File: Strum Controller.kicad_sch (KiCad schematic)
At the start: 18 parts, among them J1 USB_C_Receptacle_USB2.0, U1 RP2040, U2 NCP1117-3.3_SOT223

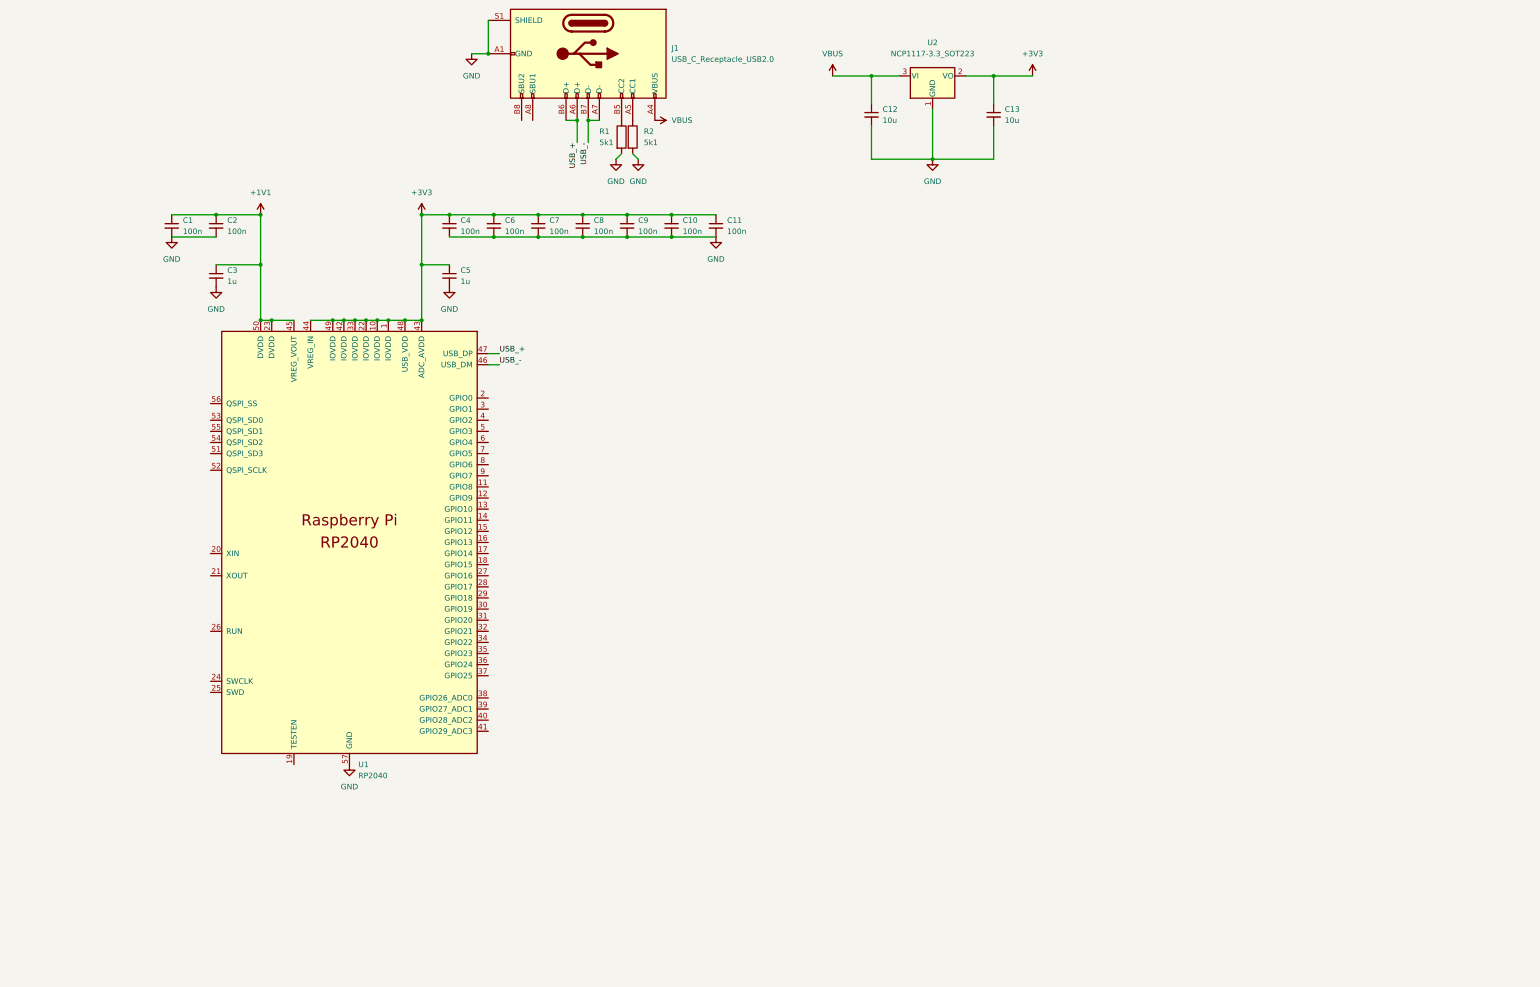
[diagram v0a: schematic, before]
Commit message: Restart design using modified RP2040 minimal design from RasPi Foundation
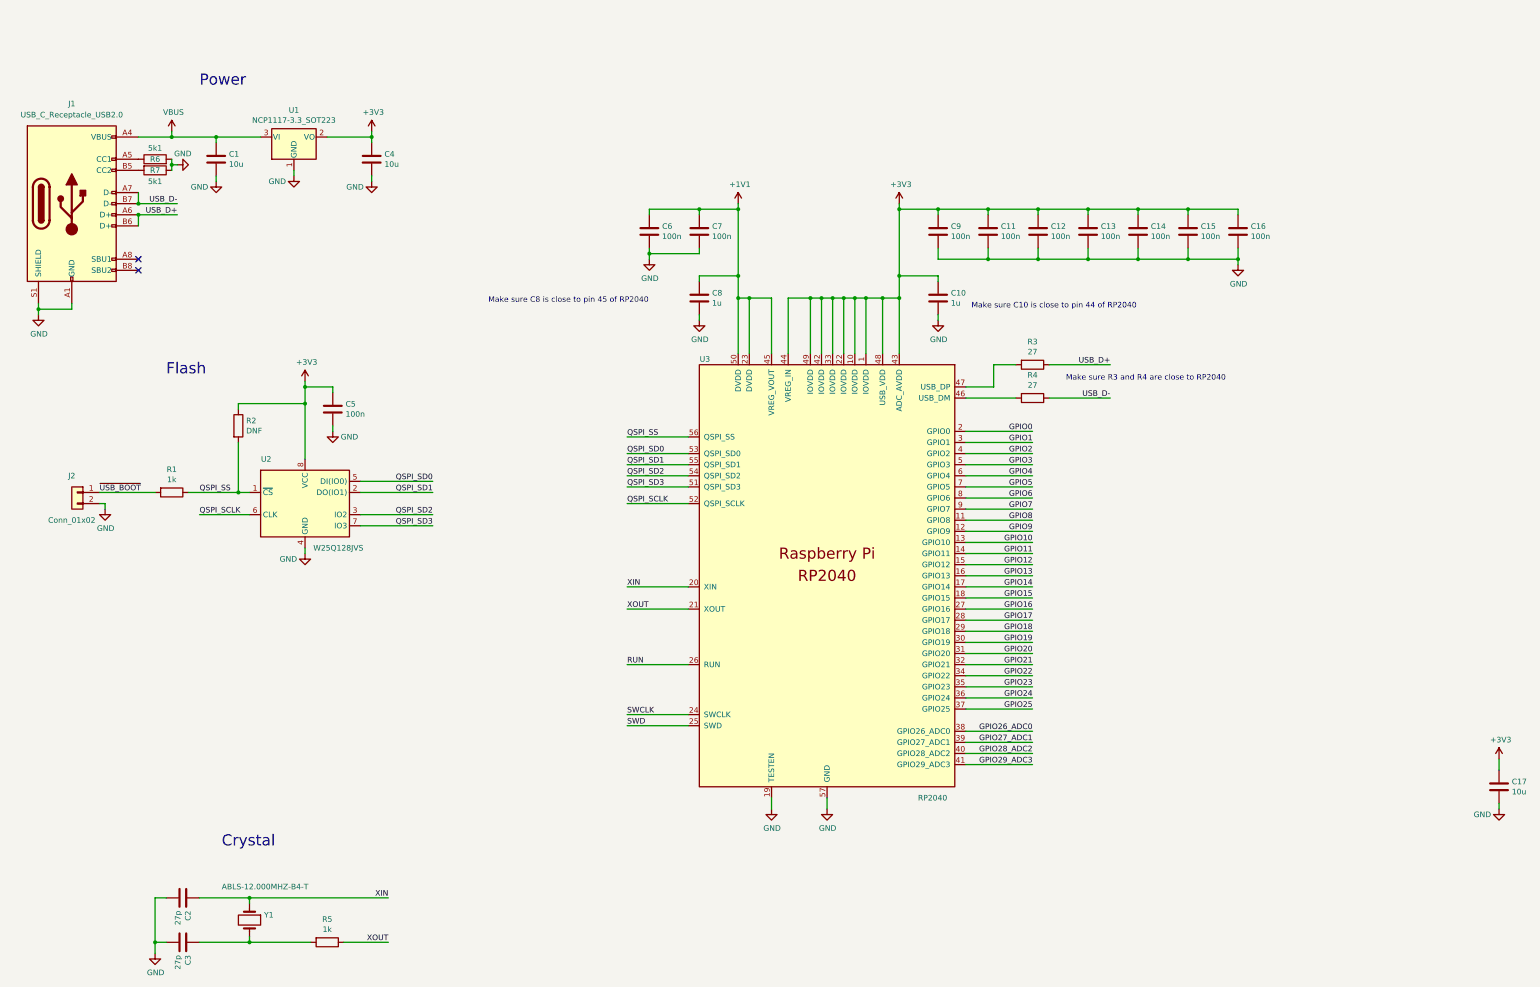
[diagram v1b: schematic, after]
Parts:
- removed C1, C10, C11, C2, C4, C6, C7, C8, C9: 100n, Capacitor_SMD:C_0402_1005Metric, symbol Device:C_Small
- removed C12, C13: 10u, Capacitor_SMD:C_0402_1005Metric, symbol Device:C_Small
- removed C3, C5: 1u, Capacitor_SMD:C_0402_1005Metric, symbol Device:C_Small
- removed U1: RP2040, kicad-rp2040:RP2040_QFN-56_EP_7x7_Pitch0.4mm_ThermalVias, symbol kicad-rp2040:RP2040
- removed U2: NCP1117-3.3_SOT223, Package_TO_SOT_SMD:SOT-223-3_TabPin2, symbol Regulator_Linear:NCP1117-3.3_SOT223
- added C1, C17, C4: 10u, Capacitor_SMD:C_0805_2012Metric, symbol Device:C
- added C10, C8: 1u, Capacitor_SMD:C_0402_1005Metric, symbol Device:C
- added C11, C12, C13, C14, C15, C16, C5, C6, C7, C9: 100n, Capacitor_SMD:C_0402_1005Metric, symbol Device:C
- added C2, C3: 27p, Capacitor_SMD:C_0402_1005Metric, symbol Device:C
- added J2: Conn_01x02, Connector_PinHeader_2.54mm:PinHeader_1x02_P2.54mm_Vertical, symbol Connector_Generic:Conn_01x02
- added R3, R4: 27, Resistor_SMD:R_0402_1005Metric, symbol Device:R
- added R5: 1k, Resistor_SMD:R_0402_1005Metric, symbol Device:R
- added R6, R7: 5k1, Resistor_SMD:R_0402_1005Metric, symbol Device:R
- added U1: NCP1117-3.3_SOT223, Package_TO_SOT_SMD:SOT-223-3_TabPin2, symbol Regulator_Linear:NCP1117-3.3_SOT223
- added U2: W25Q128JVS, Package_SO:SOIC-8_5.275x5.275mm_P1.27mm, symbol Memory_Flash:W25Q128JVS
- added U3: RP2040, kicad-rp2040:RP2040_QFN-56_EP_7x7_Pitch0.4mm_ThermalVias, symbol kicad-rp2040:RP2040
- added Y1: ABLS-12.000MHZ-B4-T, Crystal:Crystal_SMD_HC49-SD, symbol Device:Crystal
- J1: footprint Connector_USB:USB_C_Receptacle_HRO_TYPE-C-31-M-12 -> Connector_USB:USB_C_Receptacle_JAE_DX07S016JA1R1500
- R1: value 5k1 -> 1k; footprint Resistor_SMD:R_0201_0603Metric -> Resistor_SMD:R_0402_1005Metric
- R2: value 5k1 -> DNF; footprint Resistor_SMD:R_0201_0603Metric -> Resistor_SMD:R_0402_1005Metric
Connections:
- net +1V1: now also C6.1, C7.1, C8.1, U3.23 (DVDD), U3.45 (VREG_VOUT), U3.50 (DVDD)
- net +3V3: now also R2.1, C10.1, C11.1, C12.1, C13.1, C14.1, C15.1, C16.1, C17.1, C4.1, C5.1, C9.1, U1.2 (VO), U2.8 (VCC), U3.1 (IOVDD), U3.10 (IOVDD), U3.22 (IOVDD), U3.33 (IOVDD), U3.42 (IOVDD), U3.43 (ADC_AVDD), U3.44 (VREG_IN), U3.48 (USB_VDD), U3.49 (IOVDD)
- net GND: now also C1.2, C10.2, C11.2, C12.2, C13.2, C14.2, C15.2, C16.2, C17.2, C2.2, C3.2, C4.2, C5.2, C6.2, C7.2, C8.2, C9.2, J2.2 (Pin_2), R6.2, R7.1, U1.1 (GND), U2.4 (GND), U3.19 (TESTEN), U3.57 (GND); no longer R1.2, R2.2
- net VBUS: now also C1.1, U1.3 (VI)
- net at J1.A5 (CC1): now also R6.1; no longer R2.1
- net at J1.B5 (CC2): now also R7.2; no longer R1.1
- net USB_+ renamed USB_D+
- net USB_D+: now also R3.1
- net USB_- renamed USB_D-
- net USB_D-: now also R4.1
- new net: R4.2, U3.46 (USB_DM)
- new net: R3.2, U3.47 (USB_DP)
- new net: C3.1, R5.2, Y1.2
- new net GPIO0: U3.2 (GPIO0)
- new net GPIO1: U3.3 (GPIO1)
- new net GPIO10: U3.13 (GPIO10)
- new net GPIO11: U3.14 (GPIO11)
- new net GPIO12: U3.15 (GPIO12)
- new net GPIO13: U3.16 (GPIO13)
- new net GPIO14: U3.17 (GPIO14)
- new net GPIO15: U3.18 (GPIO15)
- new net GPIO16: U3.27 (GPIO16)
- new net GPIO17: U3.28 (GPIO17)
- new net GPIO18: U3.29 (GPIO18)
- new net GPIO19: U3.30 (GPIO19)
- new net GPIO2: U3.4 (GPIO2)
- new net GPIO20: U3.31 (GPIO20)
- new net GPIO21: U3.32 (GPIO21)
- new net GPIO22: U3.34 (GPIO22)
- new net GPIO23: U3.35 (GPIO23)
- new net GPIO24: U3.36 (GPIO24)
- new net GPIO25: U3.37 (GPIO25)
- new net GPIO26_ADC0: U3.38 (GPIO26_ADC0)
- new net GPIO27_ADC1: U3.39 (GPIO27_ADC1)
- new net GPIO28_ADC2: U3.40 (GPIO28_ADC2)
- new net GPIO29_ADC3: U3.41 (GPIO29_ADC3)
- new net GPIO3: U3.5 (GPIO3)
- new net GPIO4: U3.6 (GPIO4)
- new net GPIO5: U3.7 (GPIO5)
- new net GPIO6: U3.8 (GPIO6)
- new net GPIO7: U3.9 (GPIO7)
- new net GPIO8: U3.11 (GPIO8)
- new net GPIO9: U3.12 (GPIO9)
- new net QSPI_SCLK: U2.6 (CLK), U3.52 (QSPI_SCLK)
- new net QSPI_SD0: U2.5 (DI(IO0)), U3.53 (QSPI_SD0)
- new net QSPI_SD1: U2.2 (DO(IO1)), U3.55 (QSPI_SD1)
- new net QSPI_SD2: U2.3 (IO2), U3.54 (QSPI_SD2)
- new net QSPI_SD3: U2.7 (IO3), U3.51 (QSPI_SD3)
- new net QSPI_SS: R1.1, R2.2, U2.1 (~{CS}), U3.56 (QSPI_SS)
- new net RUN: U3.26 (RUN)
- new net SWCLK: U3.24 (SWCLK)
- new net SWD: U3.25 (SWD)
- new net XIN: C2.1, U3.20 (XIN), Y1.1
- new net XOUT: R5.1, U3.21 (XOUT)
- new net ~{USB_BOOT}: J2.1 (Pin_1), R1.2
- no-connect marks 0 -> 2
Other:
- note added: "Crystal"
- note added: "Flash"
- note added: "Make sure C10 is close to pin 44 of RP2040"
- note added: "Make sure C8 is close to pin 45 of RP2040"
- note added: "Make sure R3 and R4 are close to RP2040"
- note added: "Power"
- company: (none) -> Raspberry Pi (Trading) Ltd
- title: (none) -> RP2040 Minimal Design Example

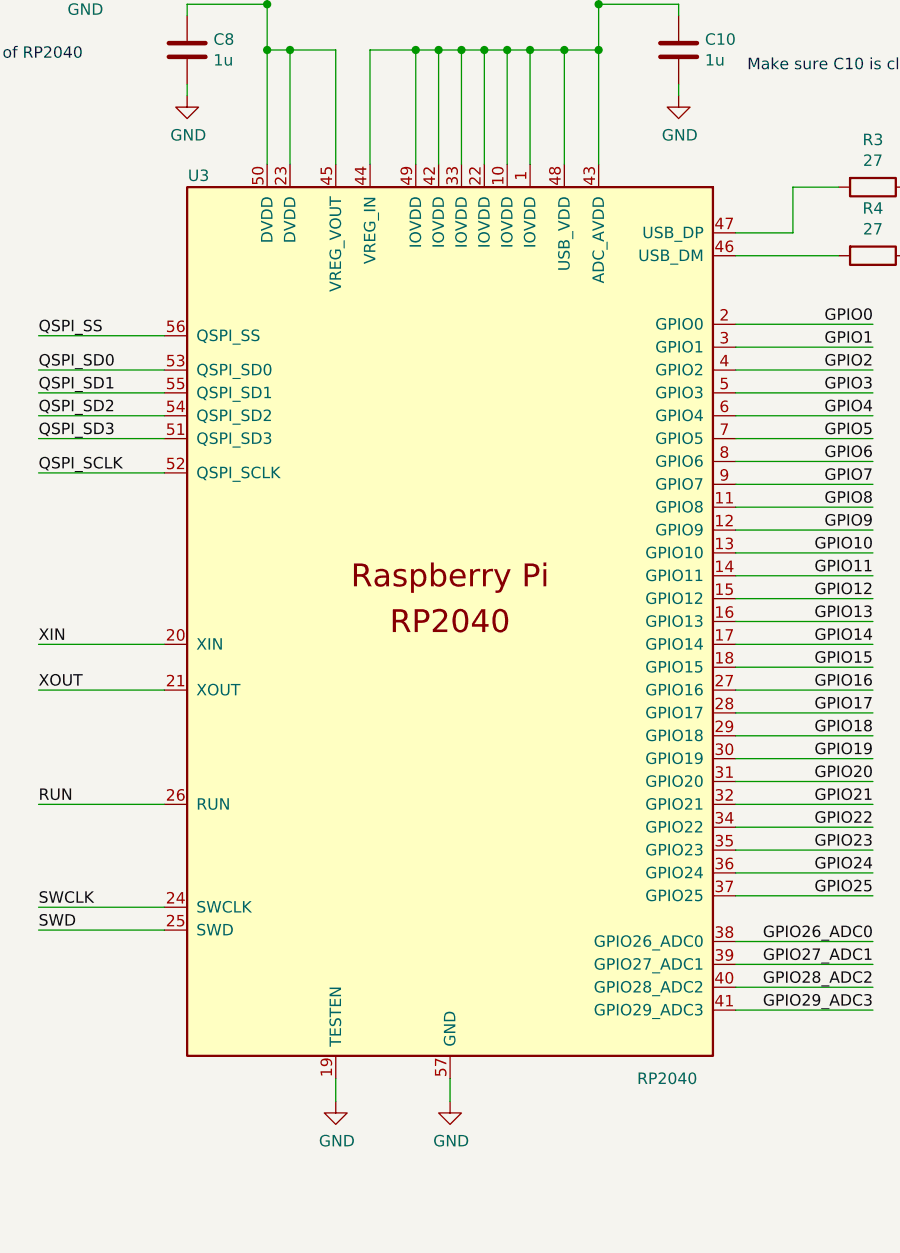
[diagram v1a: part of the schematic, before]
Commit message: Move to proper RP2040 library
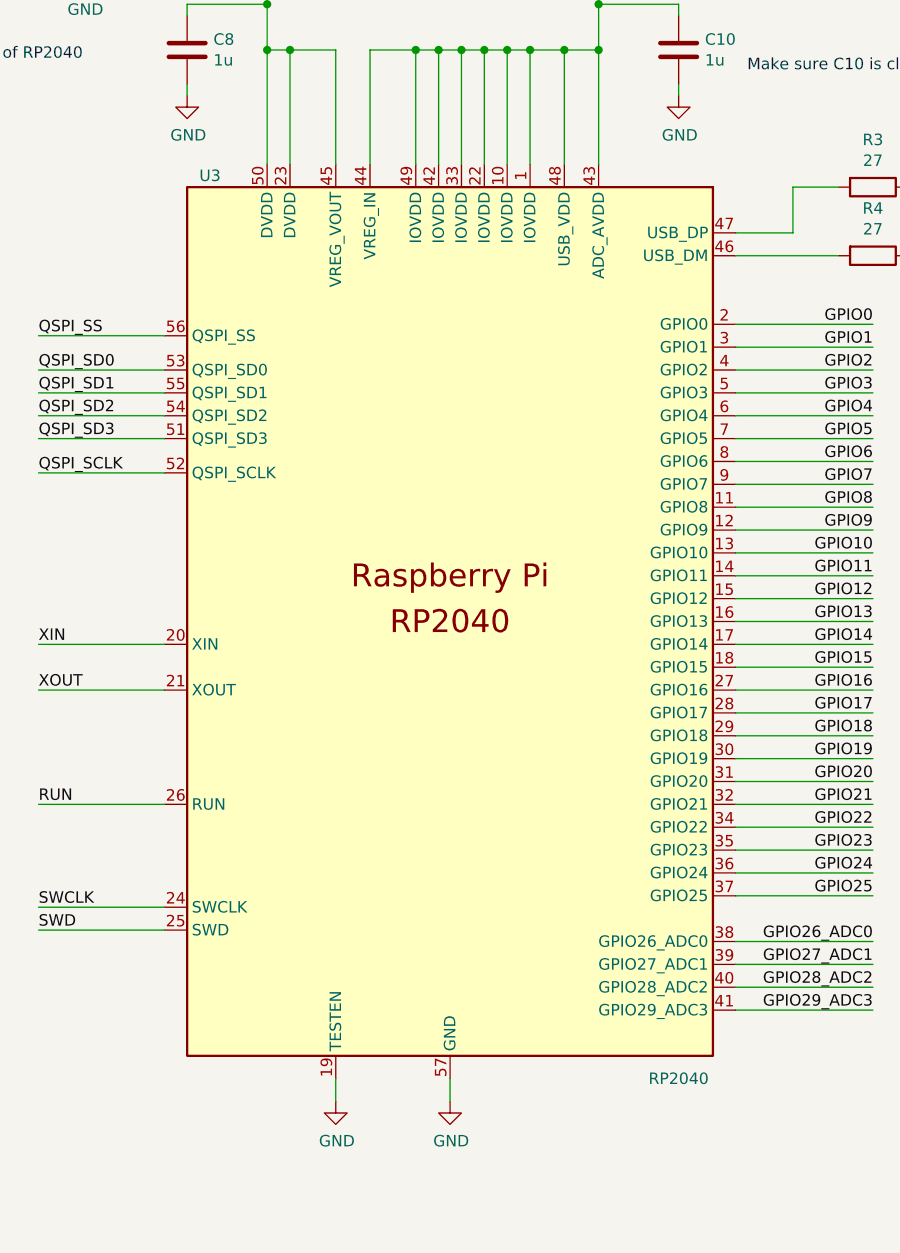
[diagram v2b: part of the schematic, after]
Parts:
- U3: footprint kicad-rp2040:RP2040_QFN-56_EP_7x7_Pitch0.4mm_ThermalVias -> kicad-lib-rp2040:QFN-56_EP_7x7_Pitch0.4mm_ThermalVias; symbol kicad-rp2040:RP2040 -> kicad-lib-rp2040:RP2040
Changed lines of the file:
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@@
     (effects (font (size 1.27 1.27)) (justify right bottom))
   )
-  (symbol (lib_id "kicad-rp2040:RP2040") (at 198.12 144.78 0) (unit 1)
-    (in_bom yes) (on_board yes)
-    (property "Reference" "U3" (id 0) (at 170.18 95.25 0))
-    (property "Value" "RP2040" (id 1) (at 222.25 195.58 0))
-    (property "Footprint" "kicad-rp2040:RP2040_QFN-56_EP_7x7_Pitch0.4mm_ThermalVias" (id 2) (at 179.07 144.78 0)
-      (effects (font (size 1.27 1.27)) hide)
-    )
-    (property "Datasheet" "https://datasheets.raspberrypi.com/rp2040/rp2040-datasheet.pdf" (id 3) (at 179.07 144.78 0)
+  (symbol (lib_id "kicad-lib-rp2040:RP2040") (at 199.39 144.78 0) (unit 1)
+    (in_bom yes) (on_board yes)
+    (property "Reference" "U3" (id 0) (at 171.45 95.25 0))
+    (property "Value" "RP2040" (id 1) (at 223.52 195.58 0))
+    (property "Footprint" "kicad-lib-rp2040:QFN-56_EP_7x7_Pitch0.4mm_ThermalVias" (id 2) (at 199.39 196.85 0)
+      (effects (font (size 1.27 1.27)) hide)
+    )
+    (property "Datasheet" "https://datasheets.raspberrypi.com/rp2040/rp2040-datasheet.pdf" (id 3) (at 199.39 194.31 0)
       (effects (font (size 1.27 1.27)) hide)
     )
@@
     )
     (path "/00000000-0000-0000-0000-00005ed8f5d6"
-      (reference "U3") (unit 1) (value "RP2040") (footprint "kicad-rp2040:RP2040_QFN-56_EP_7x7_Pitch0.4mm_ThermalVias")
+      (reference "U3") (unit 1) (value "RP2040") (footprint "kicad-lib-rp2040:QFN-56_EP_7x7_Pitch0.4mm_ThermalVias")
     )
     (path "/00000000-0000-0000-0000-00005f0dd35c"
